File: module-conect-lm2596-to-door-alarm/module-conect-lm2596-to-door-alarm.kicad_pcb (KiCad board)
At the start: 2 copper layers, 34 x 20 mm, 11 parts, among them P1 IN1, P2 IN2, P3 CONN_01X03, U1 OPTO

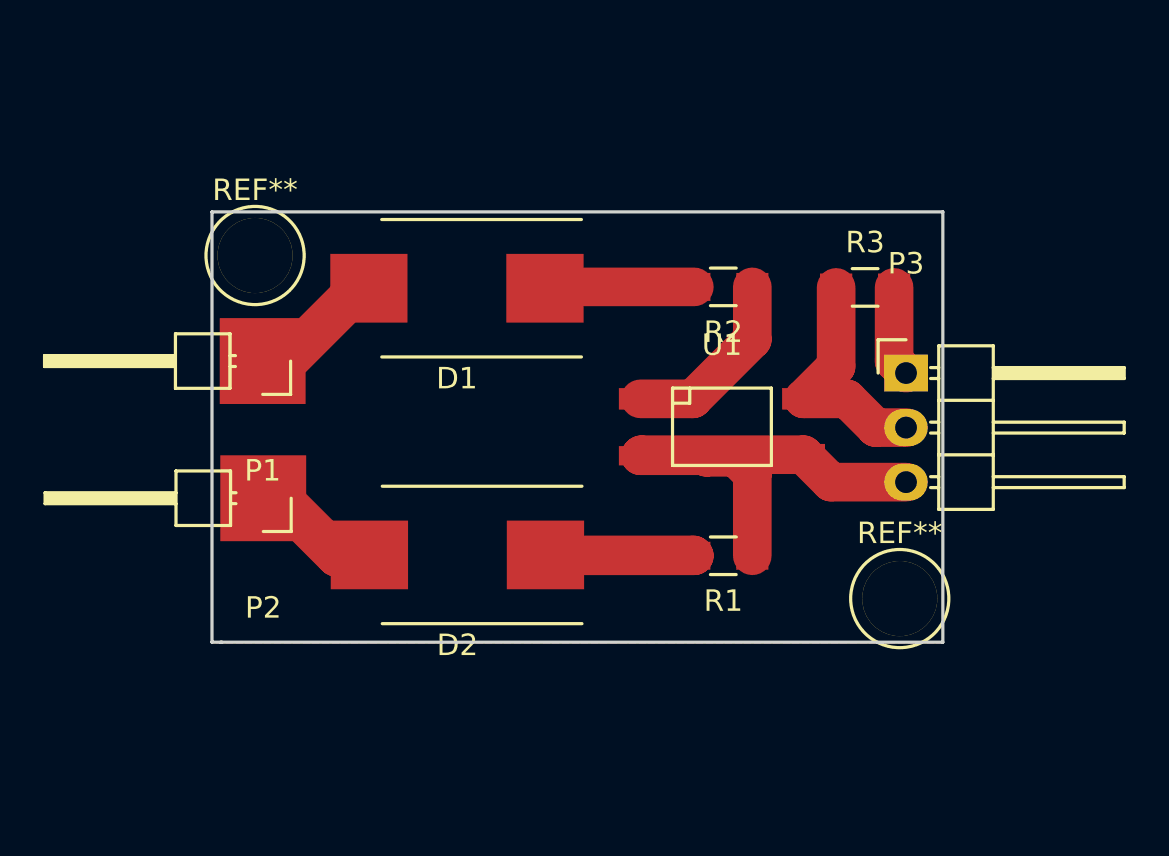
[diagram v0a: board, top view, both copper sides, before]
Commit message: edit footring header
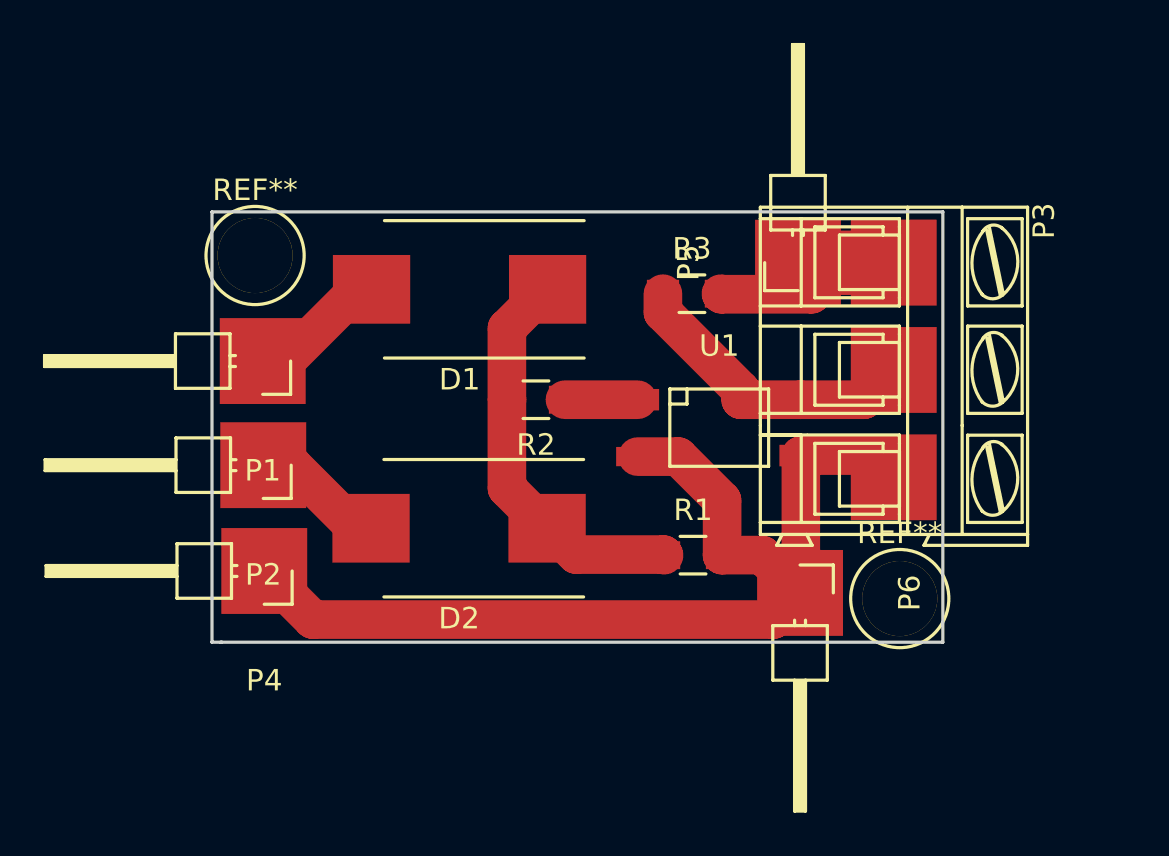
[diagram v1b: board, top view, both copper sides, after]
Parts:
- added P4: IN3, Pin_Headers:Pin_Header_Angled_1x01, F.Cu at (77.9, 129.8)
- added P5: Vcc, Pin_Headers:Pin_Header_Angled_1x01, F.Cu at (102.7, 115.4)
- added P6: GND, Pin_Headers:Pin_Header_Angled_1x01, F.Cu at (102.8, 130.8)
- P3: footprint Pin_Headers:Pin_Header_Angled_1x03 -> Connect:AK300-3
- moved R2 10.2 mm to (90.5, 121.8)
- moved R3 8.07 mm to (97.8, 116.8)
- moved P3 5.18 mm to (107.2, 115.4), turned to 270 degrees
- moved P2 1.54 mm to (77.8, 124.8)
- moved R1 1.41 mm to (97.8, 129.0), turned to 0 degrees
- moved D2 1.25 mm to (86.9, 127.8)
- moved D1 0.14 mm to (87.0, 116.6)
- moved U1 0.13 mm to (99.1, 123.1)
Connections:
- R1 pad 1: GND -> Net-(D1-Pad1)
- R1 pad 2: Net-(D1-Pad1) -> GND
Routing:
- net GND: track 22.3 -> 50.9 mm
- net +12V: track 4.22 -> 10.4 mm
- net Net-(R2-Pad1): track 8.81 -> 3.38 mm
- net Net-(P3-Pad2): track 11.1 -> 14.1 mm
- net Net-(D1-Pad1): track 20.9 -> 18.7 mm

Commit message: module conect lm2596 to door alarm Version 1.1
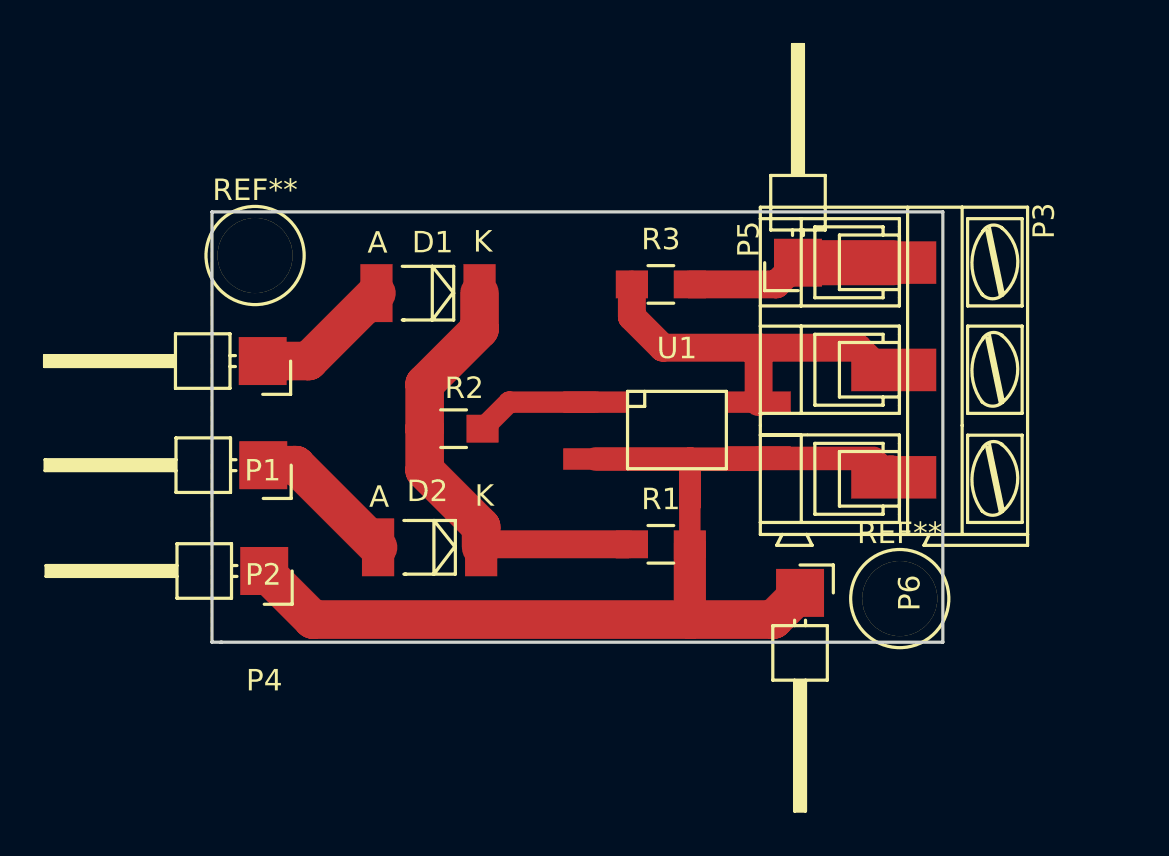
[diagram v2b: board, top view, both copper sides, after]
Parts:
- D1, D2: footprint Diodes_SMD:DO-214AB_Handsoldering -> Diodes_SMD:MELF_Standard
- moved R2 4.07 mm to (86.7, 123.1)
- moved U1 1.97 mm to (97.1, 123.2)
- moved D2 1.63 mm to (85.6, 128.7)
- moved R1 1.58 mm to (96.3, 128.5)
- moved R3 1.51 mm to (96.3, 116.4)
- moved D1 1.48 mm to (85.5, 116.8)
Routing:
- net Net-(P3-Pad2): track 14.1 -> 17.3 mm
- net Net-(R2-Pad1): track 3.38 -> 5.76 mm
- net Net-(D1-Pad1): track 18.7 -> 21.1 mm
- net Net-(D2-Pad2): track 6.23 -> 6.93 mm
- net +12V: track 10.4 -> 9.92 mm
